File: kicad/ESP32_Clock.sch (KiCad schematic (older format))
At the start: 1 part

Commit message: Board design almost ready for fabrication
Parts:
- added C1, C2: 4.7uF, Capacitors_SMD:C_0805_HandSoldering, symbol C
- added C3: 1uF, Capacitors_SMD:C_0805_HandSoldering, symbol C
- added C4, C7, C9: 100nF, Capacitors_SMD:C_0603_HandSoldering, symbol C
- added C45: CP, Capacitors_THT:CP_Radial_D8.0mm_P3.50mm, symbol CP
- added C5, C6, C8: 10uF, Capacitors_SMD:C_0805_HandSoldering, symbol C
- added D1, D2: LED, LEDs:LED_0603_HandSoldering, symbol LED
- added D3: (no value), Diodes_SMD:D_SMA_Handsoldering, symbol D_Schottky
- added J1: Battery, Connectors_JST:JST_PH_S2B-PH-K_02x2.00mm_Angled, symbol Conn_01x02
- added J12: FTDI, Pin_Headers:Pin_Header_Straight_1x06_Pitch2.54mm, symbol Conn_01x06
- added J2: LEDs, Pin_Headers:Pin_Header_Straight_1x03_Pitch2.54mm, symbol Conn_01x03
- added J3: PWR, Pin_Headers:Pin_Header_Straight_1x04_Pitch2.54mm, symbol Conn_01x04
- added J4: Grove 1, Pin_Headers:Pin_Header_Straight_1x04_Pitch2.54mm, symbol Conn_01x04
- added J5: Grove 2, Pin_Headers:Pin_Header_Straight_1x04_Pitch2.54mm, symbol Conn_01x04
- added J6: Grove 3, Pin_Headers:Pin_Header_Straight_1x04_Pitch2.54mm, symbol Conn_01x04
- added J7: Grove 4, Pin_Headers:Pin_Header_Straight_1x04_Pitch2.54mm, symbol Conn_01x04
- added J8: USB_OTG, MicroUSB_Custom:MicroUSB, symbol USB_OTG
- added Q1: NXP2301P, TO_SOT_Packages_SMD:SOT-23, symbol BSS83P
- added Q2: BCM857, TO_SOT_Packages_SMD:SOT-363_SC-70-6_Handsoldering, symbol Q_DUAL_PNP_PNP_E1B1C2E2B2C1
- added Q3: UMH3N, TO_SOT_Packages_SMD:SOT-363_SC-70-6_Handsoldering, symbol Q_DUAL_NPN_NPN_E1B1C2E2B2C1
- added R1, R3: 10k, Resistors_SMD:R_0603_HandSoldering, symbol R
- added R10, R9: 1k, Resistors_SMD:R_0603_HandSoldering, symbol R
- added R2: 2k, Resistors_SMD:R_0603_HandSoldering, symbol R
- added R4: 47k, Resistors_SMD:R_0603_HandSoldering, symbol R
- added R5, R6, R7, R8: 4k7, Resistors_SMD:R_0603_HandSoldering, symbol R
- added SW1: Reset, Buttons_Switches_SMD:SW_SPST_EVPBF, symbol SW_Push
- added SW2: Program, Buttons_Switches_SMD:SW_SPST_EVPBF, symbol SW_Push
- added U1: MCP73831, TO_SOT_Packages_SMD:SOT-23-5_HandSoldering, symbol MCP73831
- added U3: BA33DD0WHFP, LDO:LDO, symbol BA33DD0WHFP
- added U4: CP2104, QFN-24:QFN-24, symbol CP2104
- gave numbers to parts that had none: 1
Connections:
- net GND: now reaches U2.1 (GND)
- net GND: now also U2.15 (GND), U2.38 (GND), U2.39 (GND-PAD), C1.2, C2.2, C3.2, C4.2, C45.2, C5.2, C6.2, C7.2, C8.2, C9.2, J1.2 (Pin_2), J12.6 (Pin_6), J2.3 (Pin_3), J3.4 (Pin_4), J4.4 (Pin_4), J5.4 (Pin_4), J6.4 (Pin_4), J7.4 (Pin_4), J8.5 (GND), J8.6 (Shield), R2.2, R3.2, R4.2, R7.2, R8.2, SW1.2, SW2.2, U1.2 (VSS), U3.3 (GND), U4.2 (GND), U4.25 (PAD)
- net IO25: now reaches U2.10 (IO25)
- net IO26: now reaches U2.11 (IO26)
- net IO26: now also J6.1 (Pin_1)
- net IO27: now reaches U2.12 (IO27)
- net IO27: now also J6.2 (Pin_2)
- net IO14: now reaches U2.13 (IO14)
- net IO14: now also J7.2 (Pin_2)
- net IO12: now reaches U2.14 (IO12)
- net IO12: now also J7.1 (Pin_1)
- net at U2.16 (IO13): now also D1.1 (K)
- net +3V3: now reaches U2.2 (3V3)
- net +3V3: now also C45.1, C5.1, C6.1, C7.1, C8.1, C9.1, J12.4 (Pin_4), J2.1 (Pin_1), J3.3 (Pin_3), J4.3 (Pin_3), J5.3 (Pin_3), J6.3 (Pin_3), J7.3 (Pin_3), R1.1, R10.1, R9.2, U3.4 (VOUT), U4.5 (VIO), U4.6 (VDD), U4.7 (REGIN)
- net at U2.23 (IO15): now also D2.1 (K)
- net IO0: now reaches U2.25 (IO0)
- net IO0: now also Q3.3 (C2), SW2.1
- net IO4: now reaches U2.26 (IO4)
- net IO16: now reaches U2.27 (IO16)
- net IO17: now reaches U2.28 (IO17)
- net IO5: now reaches U2.29 (IO5)
- net EN: now reaches U2.3 (EN)
- net EN: now also C3.1, Q3.6 (C1), R1.2, SW1.1
- net IO18: now reaches U2.30 (IO18)
- net IO18: now also J5.1 (Pin_1)
- net IO19: now reaches U2.31 (IO19)
- net IO19: now also J5.2 (Pin_2)
- net IO21: now reaches U2.33 (IO21)
- net RXD0: now reaches U2.34 (RXD0)
- net RXD0: now also J12.3 (Pin_3), U4.21 (TXD)
- net TXD0: now reaches U2.35 (TXD0)
- net TXD0: now also J12.2 (Pin_2), U4.20 (RXD)
- net IO22: now reaches U2.36 (IO22)
- net IO22: now also J4.1 (Pin_1)
- net IO23: now reaches U2.37 (IO23)
- net IO23: now also J4.2 (Pin_2)
- net VP: now reaches U2.4 (SENSOR_VP)
- net VP: now also R6.2, R8.1
- net VN: now reaches U2.5 (SENSOR_VN)
- net VN: now also R5.2, R7.1
- net IO32: now reaches U2.8 (IO32)
- net IO33: now reaches U2.9 (IO33)
- new net: Q2.2 (B1), Q2.5 (B2), Q2.6 (C1), R3.1
- new net: Q1.1 (G), Q2.3 (C2), R4.1
- new net: R2.1, U1.5 (PROG)
- new net: D1.2 (A), R9.1
- new net: D2.2 (A), R10.2
- new net +5V: C1.1, C4.1, D3.1 (K), J3.1 (Pin_1), Q1.2 (S), Q2.4 (E2), R6.1, U1.4 (VDD), U3.1 (CTL), U3.2 (VCC)
- new net D+: J8.3 (D+), U4.3 (D+)
- new net D-: J8.2 (D-), U4.4 (D-)
- new net DTR: J12.1 (Pin_1), Q3.2 (B1), Q3.4 (E2), U4.23 (DTR)
- new net LEDs/DOUT: J2.2 (Pin_2)
- new net RTS: Q3.1 (E1), Q3.5 (B2), U4.19 (RTS)
- new net VBAT: C2.1, D3.2 (A), J1.1 (Pin_1), J3.2 (Pin_2), R5.1, U1.3 (VBAT)
- new net VBUS: J8.1 (VBUS), Q1.3 (D), Q2.1 (E1), U4.8 (VBUS)
- no-connect marks 0 -> 25
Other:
- note added: "IO25 - SDA for Gesture\nIO26 - SCL for Gesture\nIO27 - Interrupt for Gesture\n\nIO18 - SDA for Accelerometer\nIO19 - SCL for Accelerometer\nIO22 - Interrupt 2 for Accelerometer\nIO23 - Interrupt 1 for Accelerometer"
- moved on the sheet: U2

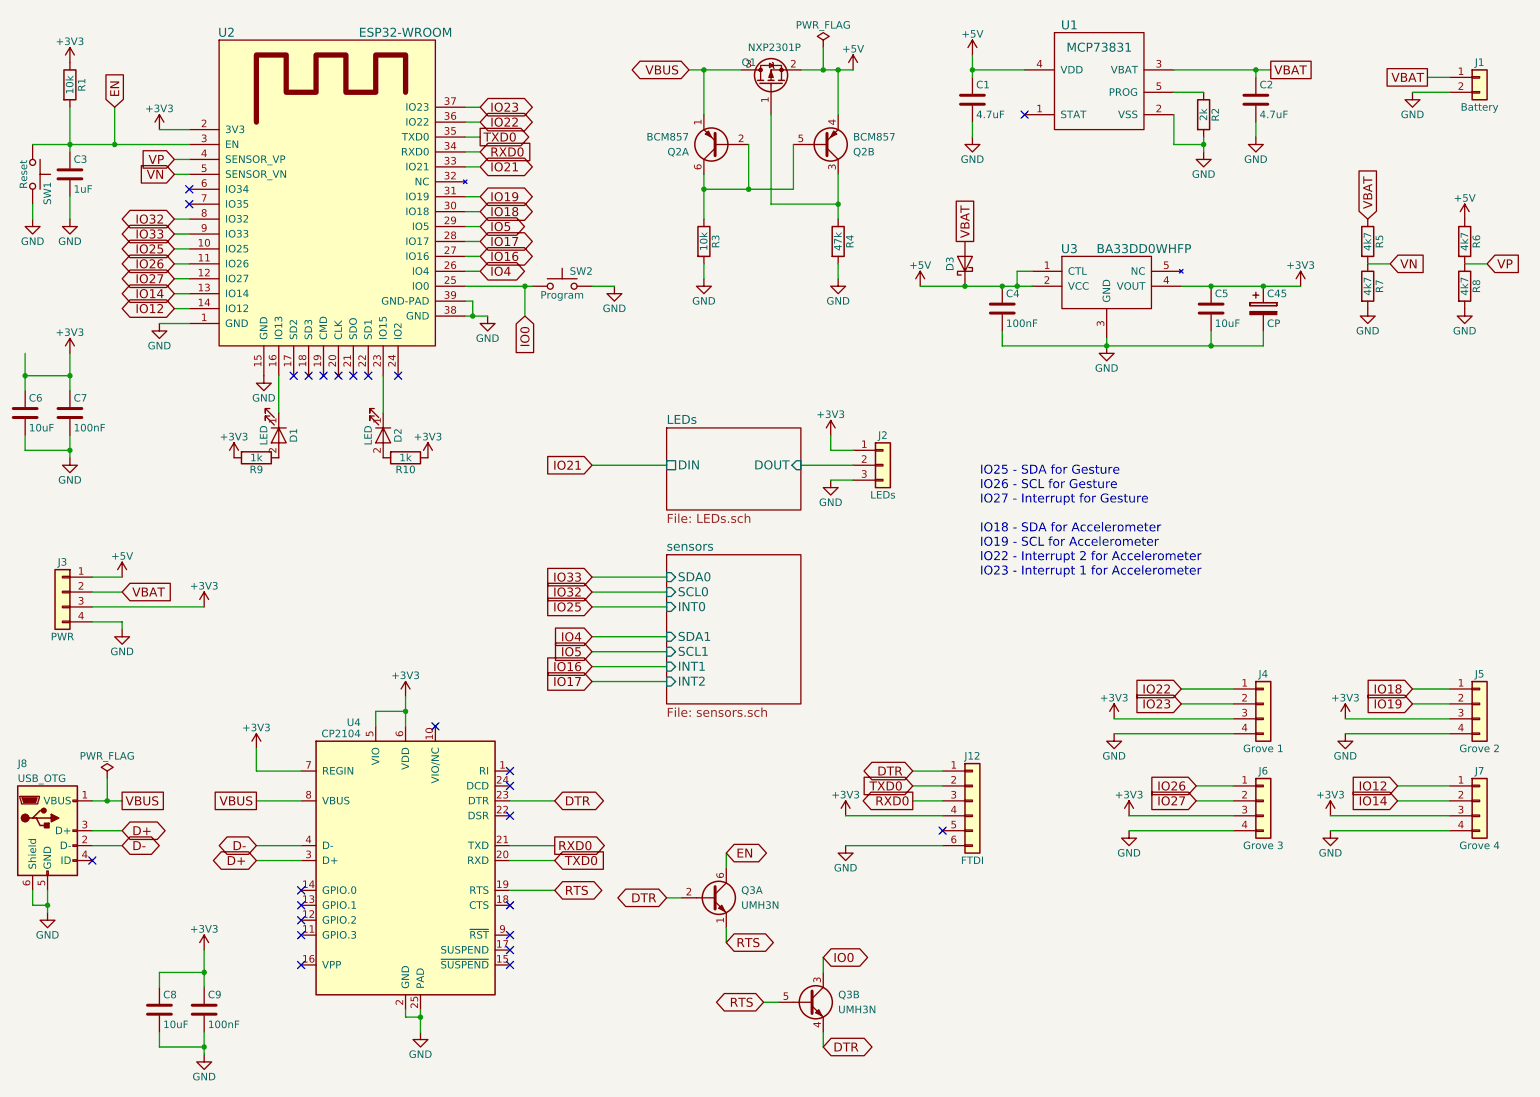
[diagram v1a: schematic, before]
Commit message: Updated hardware design and removed test idf-code
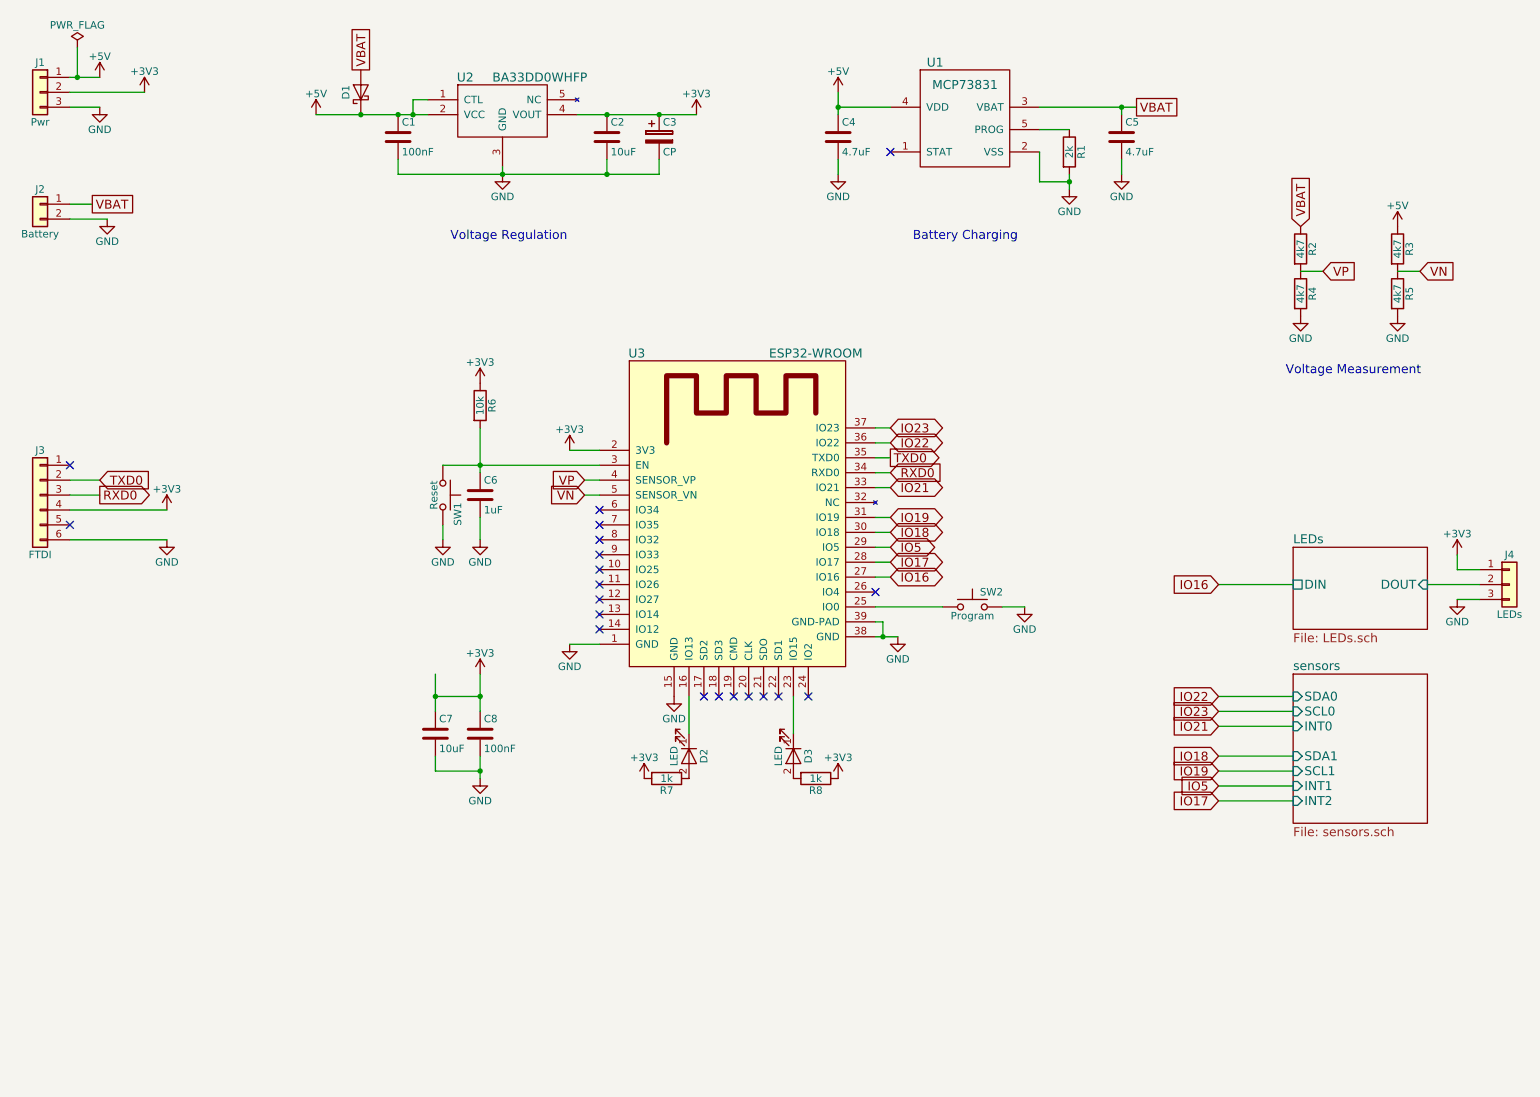
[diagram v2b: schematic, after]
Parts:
- removed C8: 10uF, Capacitors_SMD:C_0805_HandSoldering, symbol C
- removed C9: 100nF, Capacitors_SMD:C_0603_HandSoldering, symbol C
- removed J3: PWR, Pin_Headers:Pin_Header_Straight_1x04_Pitch2.54mm, symbol Conn_01x04
- removed J4: Grove 1, Pin_Headers:Pin_Header_Straight_1x04_Pitch2.54mm, symbol Conn_01x04
- removed J5: Grove 2, Pin_Headers:Pin_Header_Straight_1x04_Pitch2.54mm, symbol Conn_01x04
- removed J6: Grove 3, Pin_Headers:Pin_Header_Straight_1x04_Pitch2.54mm, symbol Conn_01x04
- removed J7: Grove 4, Pin_Headers:Pin_Header_Straight_1x04_Pitch2.54mm, symbol Conn_01x04
- removed J8: USB_OTG, MicroUSB_Custom:MicroUSB, symbol USB_OTG
- removed Q1: NXP2301P, TO_SOT_Packages_SMD:SOT-23, symbol BSS83P
- removed Q2: BCM857, TO_SOT_Packages_SMD:SOT-363_SC-70-6_Handsoldering, symbol Q_DUAL_PNP_PNP_E1B1C2E2B2C1
- removed Q3: UMH3N, TO_SOT_Packages_SMD:SOT-363_SC-70-6_Handsoldering, symbol Q_DUAL_NPN_NPN_E1B1C2E2B2C1
- removed R3: 10k, Resistors_SMD:R_0603_HandSoldering, symbol R
- removed R4: 47k, Resistors_SMD:R_0603_HandSoldering, symbol R
- removed U4: CP2104, QFN-24:QFN-24, symbol CP2104
- added J1: Pwr, Pin_Headers:Pin_Header_Straight_1x03_Pitch2.54mm, symbol Conn_01x03
- renumbered C4 to C1, C5 to C2, C45 to C3, C1 to C4, C2 to C5, C3 to C6, C6 to C7, C7 to C8, D3 to D1, D1 to D2, D2 to D3, J1 to J2, J12 to J3, J2 to J4, R2 to R1, R5 to R2, R6 to R3, R7 to R4, R8 to R5, R1 to R6, R9 to R7, R10 to R8, U3 to U2, U2 to U3
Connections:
- net +3V3: now also J1.2 (Pin_2)
- net +5V: now also J1.1 (Pin_1)
- net GND: now also J1.3 (Pin_3)
- net VN: now also R3.2, R5.1; no longer R2.2, R4.1
- net VP: now also R2.2, R4.1; no longer R3.2, R5.1
- net DTR: no longer names the net of J3.1 (Pin_1)
- net EN: no longer names the net of C6.1, R6.2, SW1.1, U3.3 (EN)
- net IO0: no longer names the net of SW2.1, U3.25 (IO0)
- net IO12: no longer names the net of U3.14 (IO12)
- net IO14: no longer names the net of U3.13 (IO14)
- net IO25: no longer names the net of U3.10 (IO25)
- net IO26: no longer names the net of U3.11 (IO26)
- net IO27: no longer names the net of U3.12 (IO27)
- net IO32: no longer names the net of U3.8 (IO32)
- net IO33: no longer names the net of U3.9 (IO33)
- net IO4: no longer names the net of U3.26 (IO4)
- no-connect marks 25 -> 20
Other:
- note added: "Battery Charging"
- note added: "Voltage Measurement"
- note added: "Voltage Regulation"
- note removed: "IO25 - SDA for Gesture\nIO26 - SCL for Gesture\nIO27 - Interrupt for Gesture\n\nIO18 - SDA for Accelerometer\nIO19 - SCL for Accelerometer\nIO22 - Interrupt 2 for Accelerometer\nIO23 - Interrupt 1 for Accelerometer"
- moved on the sheet: C1, C2, C3, C4, C5, C6, C7, C8, D1, D2, D3, J2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

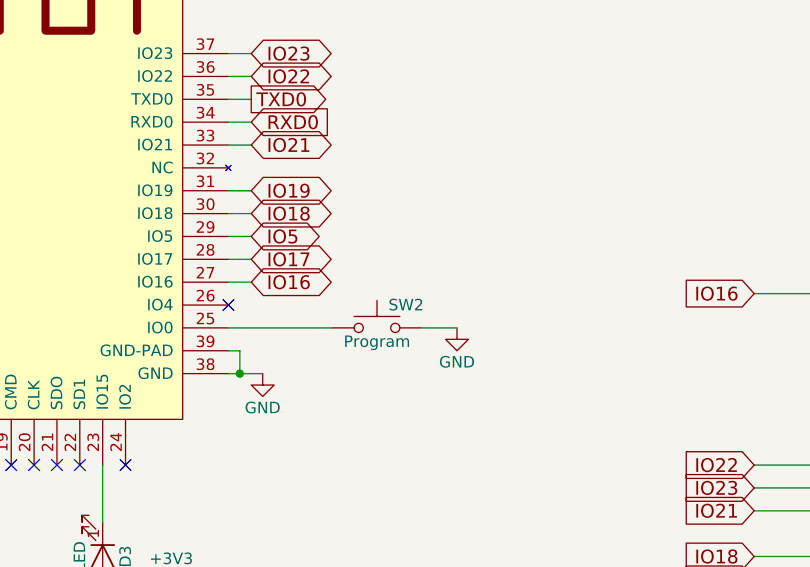
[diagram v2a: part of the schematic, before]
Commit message: Added pullup to IO0 to be safe during boot
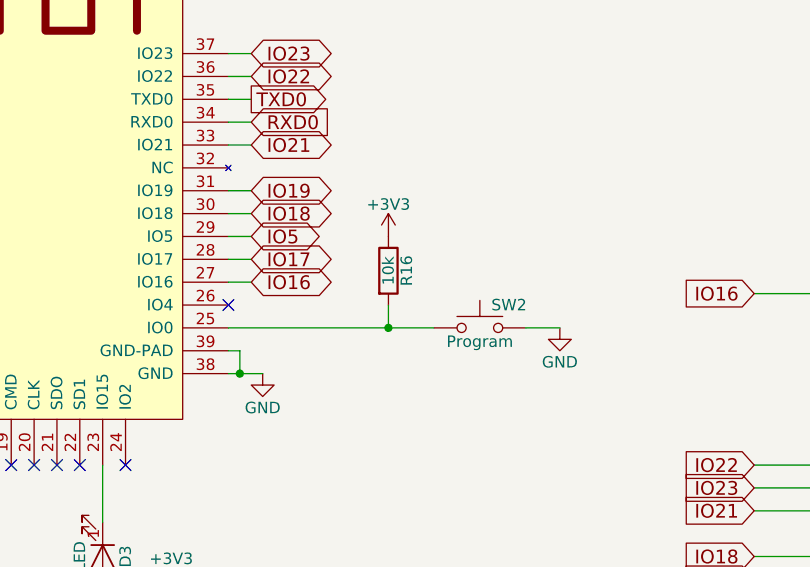
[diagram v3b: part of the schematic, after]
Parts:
- added R16: 10k, Resistors_SMD:R_0603_HandSoldering, symbol R
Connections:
- net +3V3: now also R16.1
- net at SW2.1, U3.25 (IO0): now also R16.2
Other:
- moved on the sheet: SW2
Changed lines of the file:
@@
 L SW_Push SW2
 U 1 1 5AA997A2
-P 7100 4500
-F 0 "SW2" H 7150 4600 50  0000 L CNN
-F 1 "Program" H 7100 4440 50  0000 C CNN
-F 2 "Buttons_Switches_SMD:SW_SPST_EVPBF" H 7100 4700 50  0001 C CNN
-F 3 "" H 7100 4700 50  0001 C CNN
-	1    7100 4500
+P 7550 4500
+F 0 "SW2" H 7600 4600 50  0000 L CNN
+F 1 "Program" H 7550 4440 50  0000 C CNN
+F 2 "Buttons_Switches_SMD:SW_SPST_EVPBF" H 7550 4700 50  0001 C CNN
+F 3 "" H 7550 4700 50  0001 C CNN
+	1    7550 4500
 	1    0    0    -1
 $EndComp
@@
 L GND #PWR015
 U 1 1 5AA99897
-P 7450 4500
-F 0 "#PWR015" H 7450 4250 50  0001 C CNN
-F 1 "GND" H 7450 4350 50  0000 C CNN
-F 2 "" H 7450 4500 50  0001 C CNN
-F 3 "" H 7450 4500 50  0001 C CNN
-	1    7450 4500
+P 7900 4500
+F 0 "#PWR015" H 7900 4250 50  0001 C CNN
+F 1 "GND" H 7900 4350 50  0000 C CNN
+F 2 "" H 7900 4500 50  0001 C CNN
+F 3 "" H 7900 4500 50  0001 C CNN
+	1    7900 4500
 	1    0    0    -1
 $EndComp
@@
 	6450 4300 6550 4300
 Wire Wire Line
-	6450 4500 6900 4500
+	6450 4500 7350 4500
 Wire Wire Line
 	6450 3500 6550 3500
@@
 	8750 4350 9250 4350
 Wire Wire Line
-	7300 4500 7450 4500
+	7750 4500 7900 4500
 Wire Wire Line
 	10350 4450 10500 4450
@@
 NoConn ~ 4600 4650
 NoConn ~ 6450 4400
+$Comp
+L R R16
+U 1 1 5B2E7E7A
+P 7150 4250
+F 0 "R16" V 7230 4250 50  0000 C CNN
+F 1 "10k" V 7150 4250 50  0000 C CNN
+F 2 "Resistors_SMD:R_0603_HandSoldering" V 7080 4250 50  0001 C CNN
+F 3 "" H 7150 4250 50  0001 C CNN
+	1    7150 4250
+	1    0    0    -1
+$EndComp
+Wire Wire Line
+	7150 4400 7150 4500
+Connection ~ 7150 4500
+$Comp
+L +3V3 #PWR032
+U 1 1 5B2E8270
+P 7150 4100
+F 0 "#PWR032" H 7150 3950 50  0001 C CNN
+F 1 "+3V3" H 7150 4240 50  0000 C CNN
+F 2 "" H 7150 4100 50  0001 C CNN
+F 3 "" H 7150 4100 50  0001 C CNN
+	1    7150 4100
+	1    0    0    -1
+$EndComp
 $EndSCHEMATC
